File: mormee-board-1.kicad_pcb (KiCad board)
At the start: 4 copper layers, 40 x 60 mm, 164 parts, among them J2 24FLZ-SM2-TB, J3 USB4105-GF-A, J4 S2B-PH-SM4-TB_LF__SN_, J5 DM3BT-DSF-PEJS, M1 IMP34DT05TR, M2 IMP34DT05TR, Q1 AO3401A, SW1 EVQ-PUB02K, SW2 EVQ-PUB02K, U1 W25Q128JVSIQ, U10 MAX17048G+T10, U11 MP2637GR-P, U2 RTL8735BDM-A20-N04, U3 FDS9926A, U4 FT232RNL-REEL, U5 RT8097AHGE, U6 RT8097AHGE, U7 RT9080-28GJ5, U8 RT9080-18GJ5, U9 RT9080-12GJ5

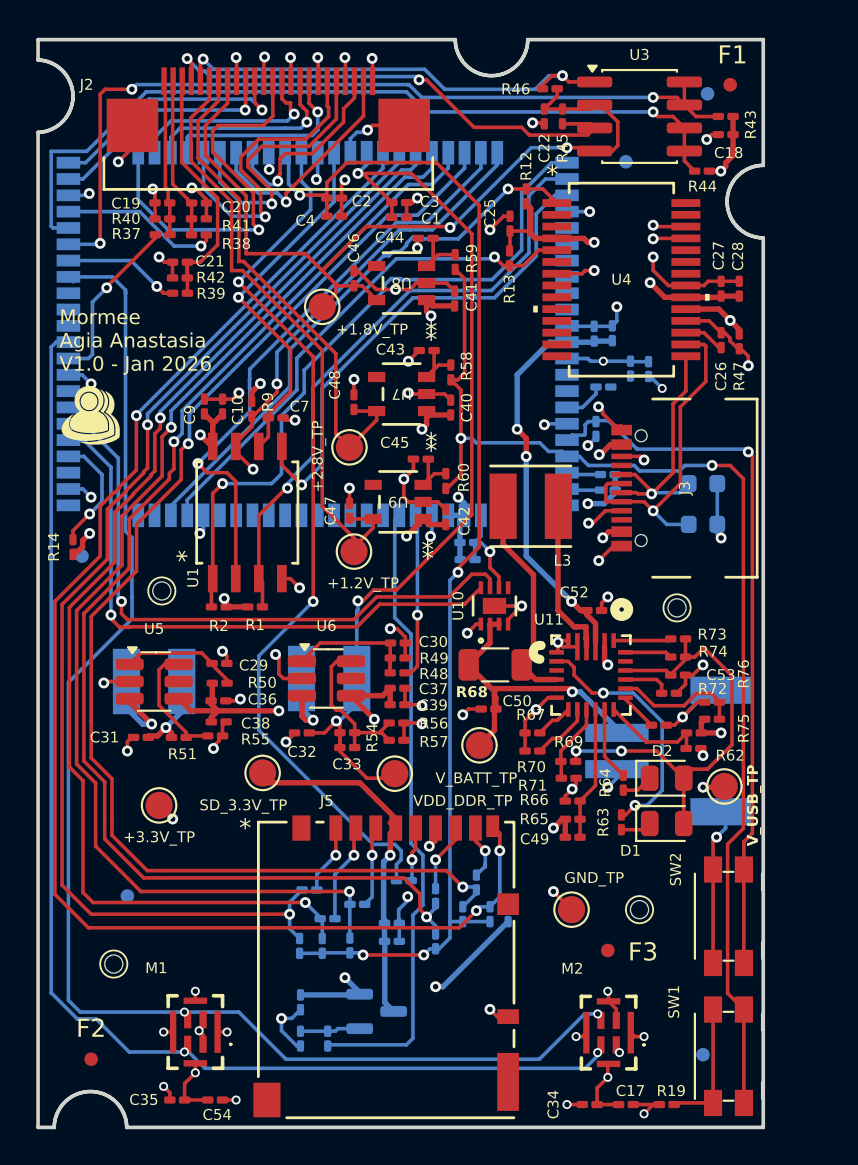
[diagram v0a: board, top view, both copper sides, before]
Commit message: Added 1k resistors in series with the FTDI Tx & Rx lines. This was recommended by Gemini to protect when the VCC is unpowered to the FTDI chip, and we're running from battery.
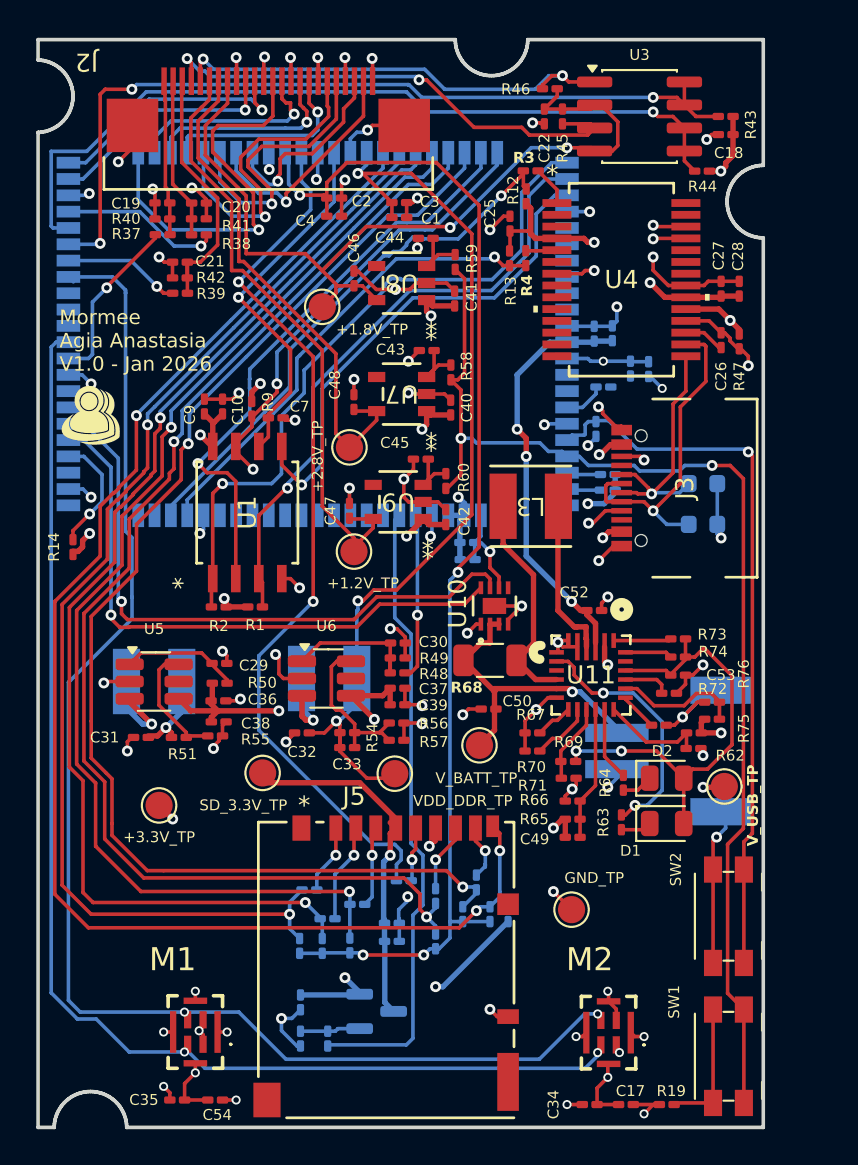
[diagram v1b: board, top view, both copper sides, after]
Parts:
- removed F1, F2, F3, F4, F5, F6, LF1, LF2: Fiducial_0.75mm_Mask1.5mm, Fiducial:Fiducial_0.75mm_Mask1.5mm
- removed MH1, MH2, MH3, MH4: MountingHole_1mm, Alignment:MountingHole_1mm
- added R3: 1K, Resistor_SMD:R_0201_0603Metric_Pad0.64x0.40mm_HandSolder, F.Cu at (96.5, 48.0)
- added R4: 1K, Resistor_SMD:R_0201_0603Metric_Pad0.64x0.40mm_HandSolder, F.Cu at (96.2, 52.8)
- moved R68 0.38 mm to (94.2, 75.0)
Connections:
- U4 pad 1: CH_UART_TX -> Net-(U4-TXD)
- U4 pad 5: CH_UART_RX -> Net-(U4-RXD)
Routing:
- net CH_UART_RX: track 28.6 -> 26.3 mm
- net Net-(U4-TXD): track 0.00 -> 2.20 mm
- net Net-(U4-RXD): track 0.00 -> 1.92 mm
- net CH_UART_TX: track 30.7 -> 30.1 mm

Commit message: Replaced all passive footprints from 0603 metric to 0603 imperial. Big oversight. All done. Next is DRC
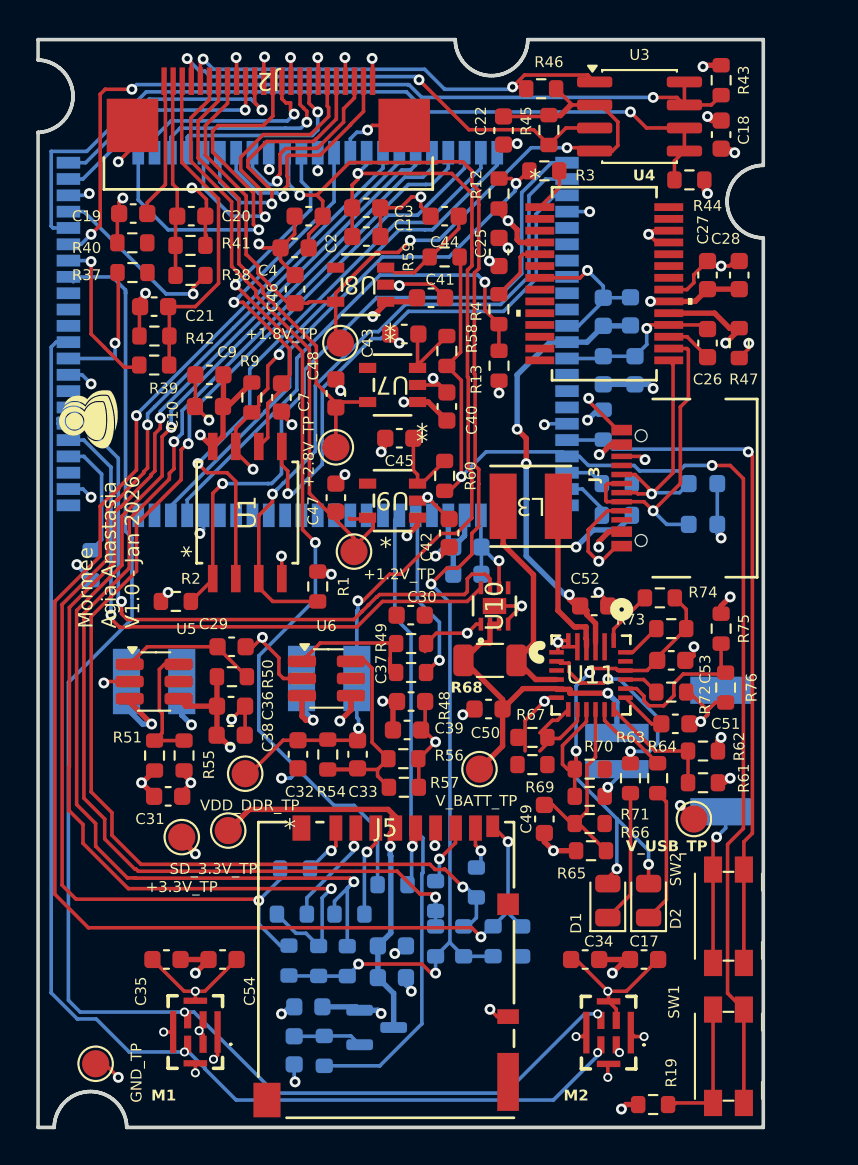
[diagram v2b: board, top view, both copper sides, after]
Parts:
- removed C5: 22uF, Capacitor_SMD:C_0201_0603Metric_Pad0.64x0.40mm_HandSolder
- C1, C11, C13, C16, C17, C18, C19, C2, C20, C22, C23, C25, C26, C27, C29, C30, C35, C36, C37, C50, C6, C9: value 0.1uF -> 0.1uF_10V; footprint Capacitor_SMD:C_0201_0603Metric_Pad0.64x0.40mm_HandSolder -> Capacitor_SMD:C_0603_1608Metric
- C10, C28: value 4.7uF -> 4.7uF_10V; footprint Capacitor_SMD:C_0201_0603Metric_Pad0.64x0.40mm_HandSolder -> Capacitor_SMD:C_0603_1608Metric
- C12, C15, C3, C31, C32, C4, C52, C8: value 10uF -> 10uF_10V; footprint Capacitor_SMD:C_0201_0603Metric_Pad0.64x0.40mm_HandSolder -> Capacitor_SMD:C_0603_1608Metric
- C14, C24, C38, C39, C40, C41, C42, C43, C44, C45, C46, C47, C48: value 2.2uF -> 2.2uF_10V; footprint Capacitor_SMD:C_0201_0603Metric_Pad0.64x0.40mm_HandSolder -> Capacitor_SMD:C_0603_1608Metric
- C21: value 0.1uF/NC -> 0.1uF_10VNC; footprint Capacitor_SMD:C_0201_0603Metric_Pad0.64x0.40mm_HandSolder -> Capacitor_SMD:C_0603_1608Metric
- C33: value 68pF -> 68pF_10V; footprint Capacitor_SMD:C_0201_0603Metric_Pad0.64x0.40mm_HandSolder -> Capacitor_SMD:C_0603_1608Metric
- C34, C54: value 1uF -> 1uF_10V; footprint Capacitor_SMD:C_0201_0603Metric_Pad0.64x0.40mm_HandSolder -> Capacitor_SMD:C_0603_1608Metric
- C49: value 120pF -> 120pF_10V; footprint Capacitor_SMD:C_0201_0603Metric_Pad0.64x0.40mm_HandSolder -> Capacitor_SMD:C_0603_1608Metric
- C51, C53: value 100nF -> 100nF_10V; footprint Capacitor_SMD:C_0201_0603Metric_Pad0.64x0.40mm_HandSolder -> Capacitor_SMD:C_0603_1608Metric
- C7: value 10pF/NC -> 0.1uF_10VNC; footprint Capacitor_SMD:C_0201_0603Metric_Pad0.64x0.40mm_HandSolder -> Capacitor_SMD:C_0603_1608Metric
- D1: value RED -> LED_2012_RED
- D2: value BLUE -> LED_2012_BLUE
- J4: value S2B-PH-SM4-TB_LF__SN_ -> S2B-PH-SM4-TB(LF)(SN)
- R1, R12, R13, R15, R16, R17, R2, R21, R36, R45, R46, R47, R48, R66, R70, R71, R9: value 10K -> 10K_1%; footprint Resistor_SMD:R_0201_0603Metric_Pad0.64x0.40mm_HandSolder -> Resistor_SMD:R_0603_1608Metric
- R14: value 10K -> 10K_1%; footprint Resistor_SMD:R_0201_0603Metric_Pad0.64x0.40mm_HandSolder -> Resistor_SMD:R_0603_1608Metric; moved to B.Cu
- R19, R3, R4: value 1K -> 1K_1%; footprint Resistor_SMD:R_0201_0603Metric_Pad0.64x0.40mm_HandSolder -> Resistor_SMD:R_0603_1608Metric
- R22, R23, R24, R26, R27, R28, R29: value 33K -> 33K_1%; footprint Resistor_SMD:R_0201_0603Metric_Pad0.64x0.40mm_HandSolder -> Resistor_SMD:R_0603_1608Metric
- R31, R32, R33, R34, R35, R58, R59, R60: value 47K -> 47K_1%; footprint Resistor_SMD:R_0201_0603Metric_Pad0.64x0.40mm_HandSolder -> Resistor_SMD:R_0603_1608Metric
- R37, R38, R43, R44: value 4.7K -> 4.7K_1%; footprint Resistor_SMD:R_0201_0603Metric_Pad0.64x0.40mm_HandSolder -> Resistor_SMD:R_0603_1608Metric
- R39: value 470 -> 470_1%; footprint Resistor_SMD:R_0201_0603Metric_Pad0.64x0.40mm_HandSolder -> Resistor_SMD:R_0603_1608Metric
- R40, R41: value 5.6K -> 5.6K_1%; footprint Resistor_SMD:R_0201_0603Metric_Pad0.64x0.40mm_HandSolder -> Resistor_SMD:R_0603_1608Metric
- R42: value 560 -> 560_1%; footprint Resistor_SMD:R_0201_0603Metric_Pad0.64x0.40mm_HandSolder -> Resistor_SMD:R_0603_1608Metric
- R49, R50: value 100K -> 100K_1%; footprint Resistor_SMD:R_0201_0603Metric_Pad0.64x0.40mm_HandSolder -> Resistor_SMD:R_0603_1608Metric
- R51, R57: value 200K/1% -> 200K_1%; footprint Resistor_SMD:R_0201_0603Metric_Pad0.64x0.40mm_HandSolder -> Resistor_SMD:R_0603_1608Metric
- R54: value 150K/1% -> 147K_1%; footprint Resistor_SMD:R_0201_0603Metric_Pad0.64x0.40mm_HandSolder -> Resistor_SMD:R_0603_1608Metric
- R55: value 44.2K/1% -> 44.RES_0603_1%_2K; footprint Resistor_SMD:R_0201_0603Metric_Pad0.64x0.40mm_HandSolder -> Resistor_SMD:R_0603_1608Metric
- R56: value 120K/1% -> 120K_1%; footprint Resistor_SMD:R_0201_0603Metric_Pad0.64x0.40mm_HandSolder -> Resistor_SMD:R_0603_1608Metric
- R61: value 15K -> 15K_1%; footprint Resistor_SMD:R_0201_0603Metric_Pad0.64x0.40mm_HandSolder -> Resistor_SMD:R_0603_1608Metric
- R62, R76: value 5.1K -> 5.1K_1%; footprint Resistor_SMD:R_0201_0603Metric_Pad0.64x0.40mm_HandSolder -> Resistor_SMD:R_0603_1608Metric
- R63, R64, R73, R74: value 2.1K -> 2.1K_1%; footprint Resistor_SMD:R_0201_0603Metric_Pad0.64x0.40mm_HandSolder -> Resistor_SMD:R_0603_1608Metric
- R65: value 31.6K -> 31.6K_1%; footprint Resistor_SMD:R_0201_0603Metric_Pad0.64x0.40mm_HandSolder -> Resistor_SMD:R_0603_1608Metric
- R67, R69: value 147K -> 147K_1%; footprint Resistor_SMD:R_0201_0603Metric_Pad0.64x0.40mm_HandSolder -> Resistor_SMD:R_0603_1608Metric
- R68: value 20m - WSL1206R0200FEA -> WSL1206R0200FEA
- R72: value 90K -> 90K_1%; footprint Resistor_SMD:R_0201_0603Metric_Pad0.64x0.40mm_HandSolder -> Resistor_SMD:R_0603_1608Metric
- R75: value 23.7K -> 23.7K_1%; footprint Resistor_SMD:R_0201_0603Metric_Pad0.64x0.40mm_HandSolder -> Resistor_SMD:R_0603_1608Metric
- moved TP9 27.6 mm to (72.5, 97.2)
- moved TP4 8.25 mm to (80.8, 81.2)
- moved C17 8.06 mm to (102.8, 91.5), turned to 180 degrees
- moved C34 8.00 mm to (99.5, 91.5), turned to 180 degrees
- moved C35 7.77 mm to (76.4, 91.5), turned to 0 degrees
- moved C54 7.76 mm to (79.5, 91.5), turned to 180 degrees
- moved D2 6.82 mm to (103.0, 88.2), turned to 90 degrees
- moved R13 5.96 mm to (94.8, 58.8), turned to 90 degrees
- moved D1 5.35 mm to (100.8, 88.2), turned to 90 degrees
- moved R75 5.02 mm to (107.0, 73.2), turned to -90 degrees
- moved R39 4.21 mm to (75.7, 58.7)
- moved TP6 3.70 mm to (79.8, 84.4)
- moved R1 3.63 mm to (84.8, 70.9), turned to -90 degrees
- moved C31 3.58 mm to (76.5, 82.5), turned to 0 degrees
- moved R42 3.50 mm to (75.7, 57.1)
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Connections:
- U2 pad 75: Net-(U2-AOUT_LP) -> unconnected-(U2-AOUT_LP-Pad75)
- U2 pad 76: /RTL9835B/MIC_BIAS -> unconnected-(U2-MICBIAS-Pad76)
- U2 pad 77: /RTL9835B/MIC1_P -> unconnected-(U2-MIC1_P-Pad77)
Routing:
- net GND: track 167.9 -> 187.5 mm, vias 83 -> 75
- net VDIO_SD: track 68.5 -> 75.2 mm
- net Net-(D2-K): track 1.73 -> 7.47 mm
- net Net-(D1-K): track 1.70 -> 7.38 mm
- net /SD CARD /Vidio / Audio / USB/EXTCLK: track 14.5 -> 18.6 mm
- net Net-(U6-FB): track 9.18 -> 13.2 mm
- net +3.3V: track 65.4 -> 61.6 mm, vias 23 -> 26
- net SD_D3: track 64.2 -> 68.0 mm
- net Net-(U11-FB): track 7.41 -> 11.2 mm
- net SD_CMD: track 65.0 -> 68.4 mm
- net SD_3V3: track 19.4 -> 22.7 mm
- net /RTL9835B/FLASH_D2: track 34.1 -> 37.2 mm
- net Net-(U11-*CHG): track 14.0 -> 11.1 mm
- net SEN_1V8: track 47.4 -> 50.3 mm
- net SEN_2V8: track 28.2 -> 25.7 mm
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
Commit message: All footprints are humanly visible (using imperial 0603), no meaningful DRC issues, and looking good.
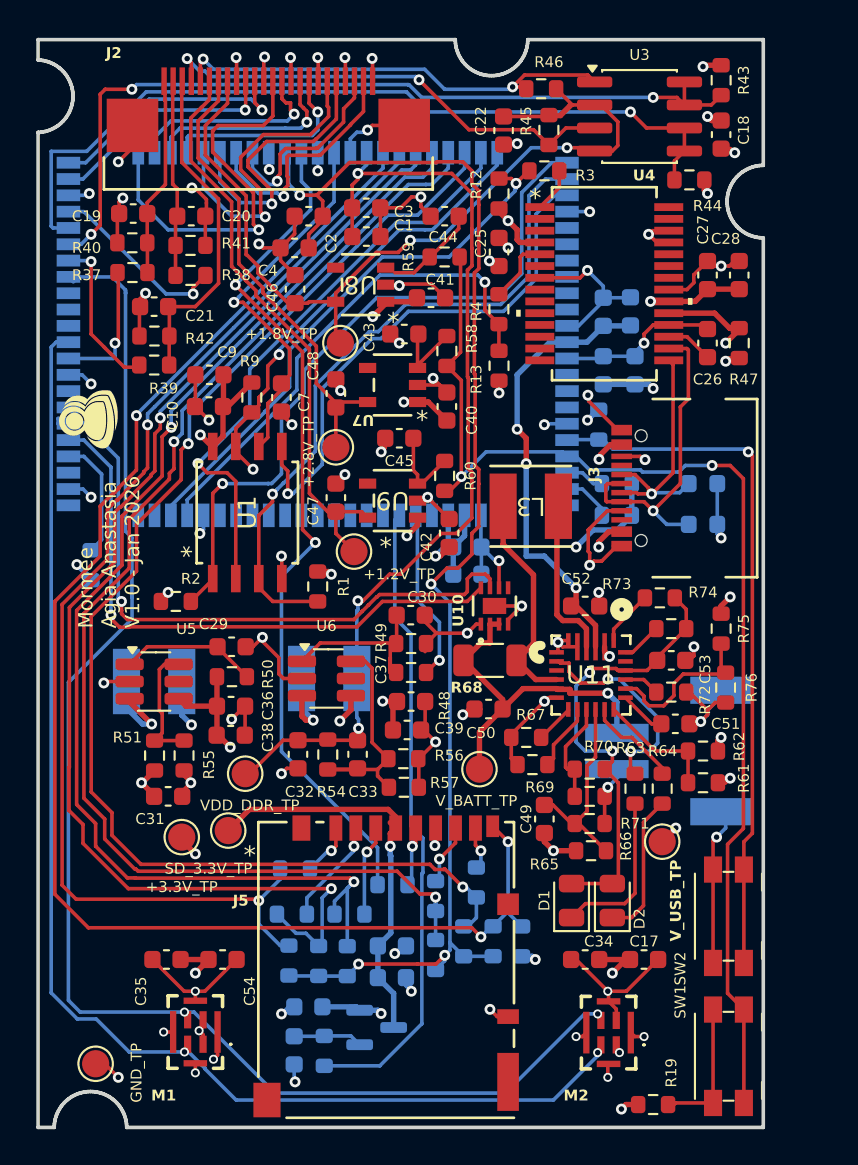
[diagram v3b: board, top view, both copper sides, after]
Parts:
- moved TP7 2.15 mm to (103.8, 85.0)
- moved D1 2.00 mm to (98.8, 88.2)
- moved D2 2.00 mm to (101.0, 88.2)
- moved R31 0.75 mm to (91.2, 91.2)
- moved R63 0.63 mm to (102.2, 82.1)
- moved R64 0.63 mm to (103.8, 82.1)
- moved C52 0.50 mm to (99.5, 72.0)
- moved R67 0.34 mm to (96.2, 79.2)
- moved R15 0.25 mm to (100.2, 62.0)
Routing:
- net GND: track 187.5 -> 193.0 mm, vias 75 -> 76
- net /SD CARD /Vidio / Audio / USB/RESETB: track 7.82 -> 11.1 mm
- net SD_CLK: track 49.9 -> 47.1 mm, vias 3 -> 2
- net +3.3V: track 61.6 -> 64.2 mm, vias 26 -> 27
- net Net-(D1-K): track 7.38 -> 9.00 mm
- net Net-(U6-EN): track 7.78 -> 9.36 mm
- net /Battery/VCC: track 26.4 -> 25.0 mm, vias 4 -> 2
- net SEN_1V2: track 33.7 -> 32.3 mm
- net V_USB: track 14.5 -> 15.3 mm, vias 7 -> 8
- net +5V: track 37.4 -> 38.2 mm
- net SD_D0: track 69.0 -> 69.7 mm
- net Net-(U11-*ACOK): track 4.51 -> 5.19 mm
- net Net-(U11-*CHG): track 11.1 -> 11.8 mm
- net Net-(D2-K): track 7.47 -> 8.05 mm
- net SD_PWR_EN: track 35.7 -> 35.2 mm

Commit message: All fiducials and mounting holes placed. Except one hole, which I'll try to place. WIP
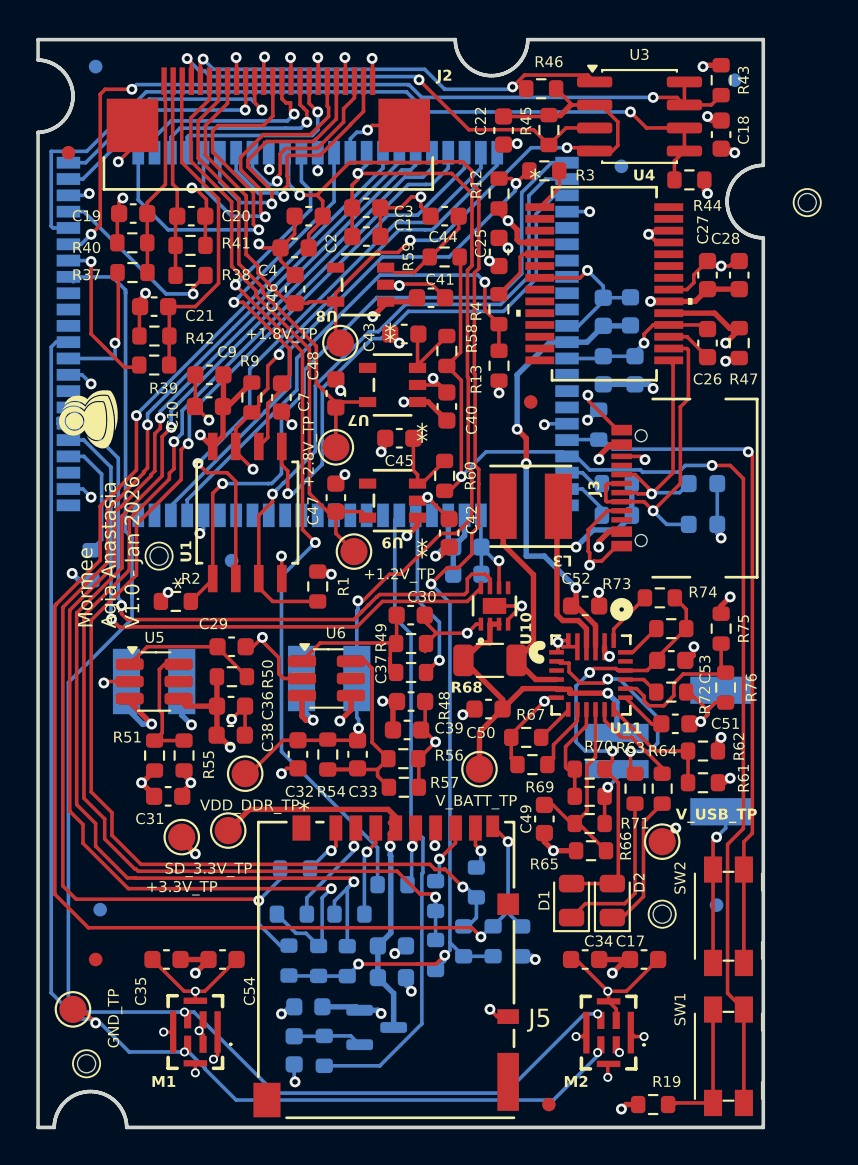
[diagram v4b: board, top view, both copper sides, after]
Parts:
- added FID1: Fiducial, Fiducial:Fiducial_0.75mm_Mask1.5mm, F.Cu at (71.0, 47.0)
- added FID10: Fiducial, Fiducial:Fiducial_0.75mm_Mask1.5mm, B.Cu at (80.0, 69.5)
- added FID2: Fiducial, Fiducial:Fiducial_0.75mm_Mask1.5mm, F.Cu at (96.5, 60.8)
- added FID3: Fiducial, Fiducial:Fiducial_0.75mm_Mask1.5mm, F.Cu at (72.5, 91.5)
- added FID4: Fiducial, Fiducial:Fiducial_0.75mm_Mask1.5mm, F.Cu at (97.5, 99.5)
- added FID5: Fiducial, Fiducial:Fiducial_0.75mm_Mask1.5mm, B.Cu at (72.5, 42.2)
- added FID6: Fiducial, Fiducial:Fiducial_0.75mm_Mask1.5mm, B.Cu at (107.8, 43.0)
- added FID7: Fiducial, Fiducial:Fiducial_0.75mm_Mask1.5mm, B.Cu at (72.8, 88.8)
- added FID8: Fiducial, Fiducial:Fiducial_0.75mm_Mask1.5mm, B.Cu at (106.8, 88.5)
- added FID9: Fiducial, Fiducial:Fiducial_0.75mm_Mask1.5mm, B.Cu at (101.5, 47.8)
- added H1: MountingHole, Alignment:MountingHole_1mm, F.Cu at (111.8, 49.8)
- added H2: MountingHole, Alignment:MountingHole_1mm, F.Cu at (76.0, 69.2)
- added H3: MountingHole, Alignment:MountingHole_1mm, F.Cu at (103.8, 89.0)
- added H4: MountingHole, Alignment:MountingHole_1mm, F.Cu at (72.0, 97.2)
- moved TP9 3.25 mm to (71.2, 94.2)

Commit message: This should be it. Gerber files with drill files generated.
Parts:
- moved H1 20.2 mm to (92.5, 43.5)
- moved FID2 14.8 mm to (92.5, 46.5)
- moved C52 1.03 mm to (99.8, 71.0), turned to -90 degrees
- moved H4 0.25 mm to (71.8, 97.2)
- turned R46 to 0 degrees
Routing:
- net /SD CARD /Vidio / Audio / USB/SDA: track 24.8 -> 30.0 mm
- net GND: track 193.0 -> 190.6 mm
- net SEN_SDA: track 45.8 -> 46.6 mm
- net /Battery/L3: track 12.2 -> 11.6 mm
- net +5V: track 38.2 -> 38.9 mm
- net SEN_SCL: track 45.3 -> 45.9 mm
